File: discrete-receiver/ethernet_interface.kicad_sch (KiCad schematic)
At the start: 16 parts, among them J6 SI-52003-F, U9 LAN8720A

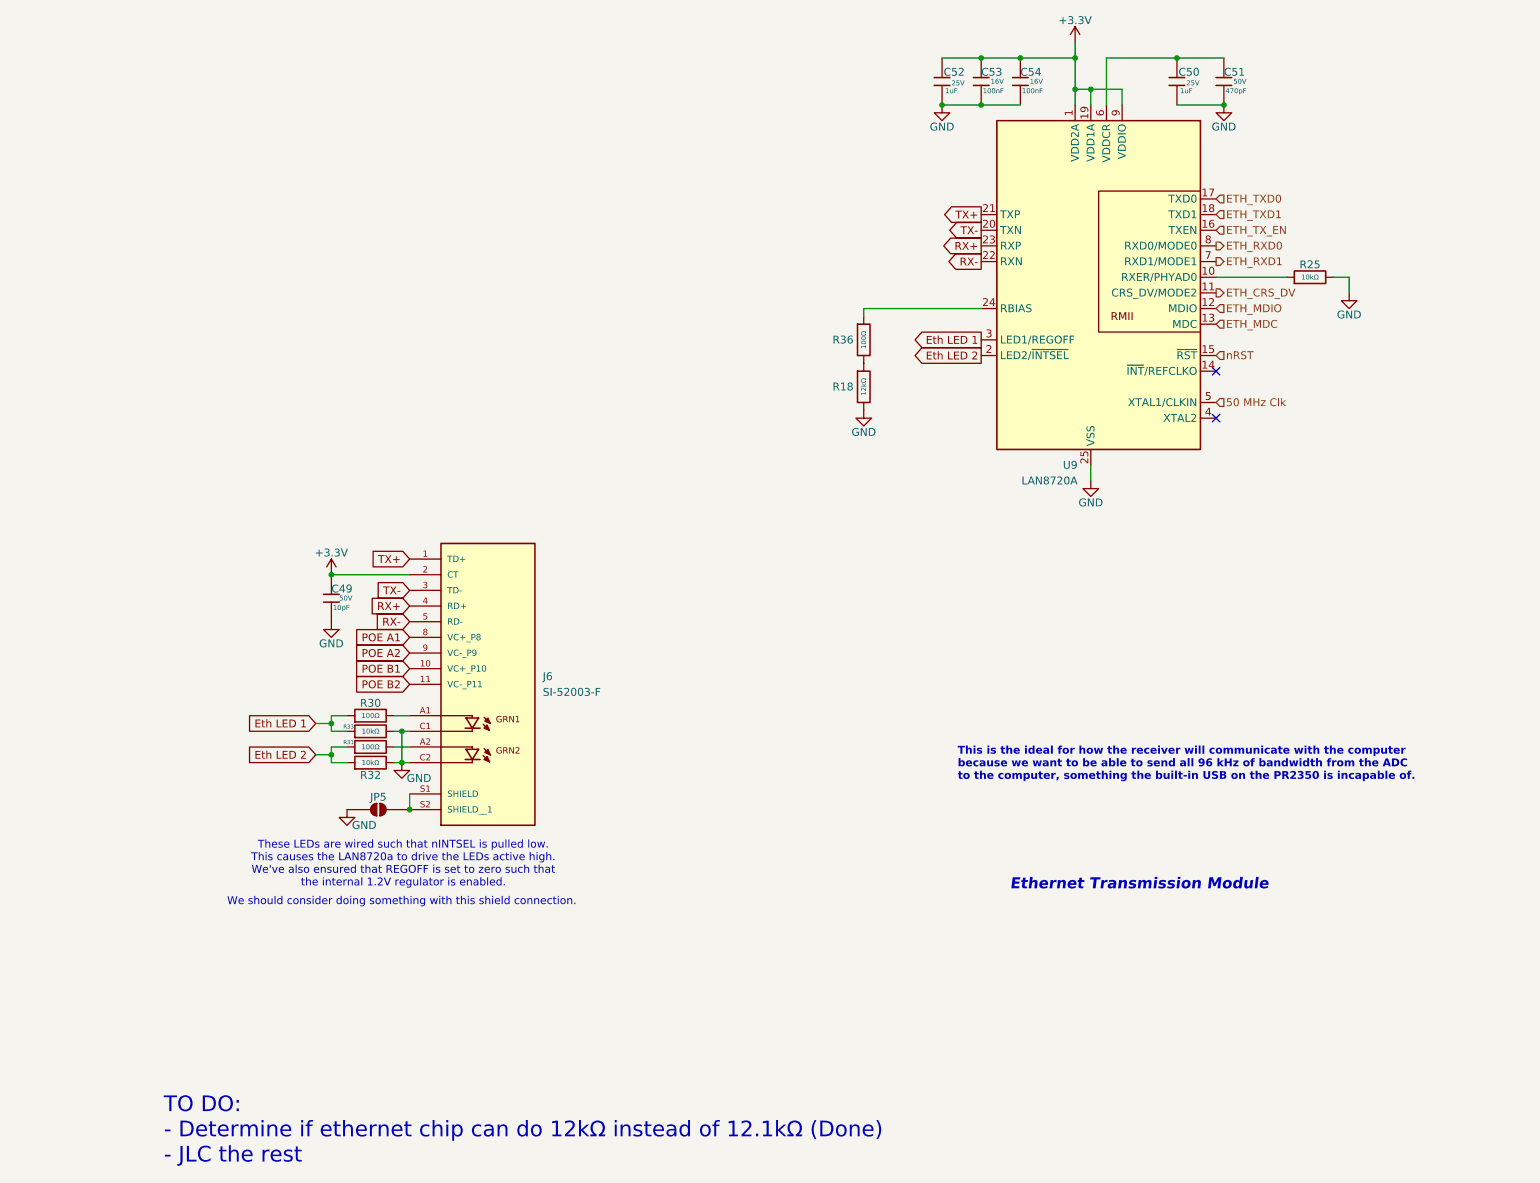
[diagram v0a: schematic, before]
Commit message: Updated JLC part numbers because some parts were out of stock
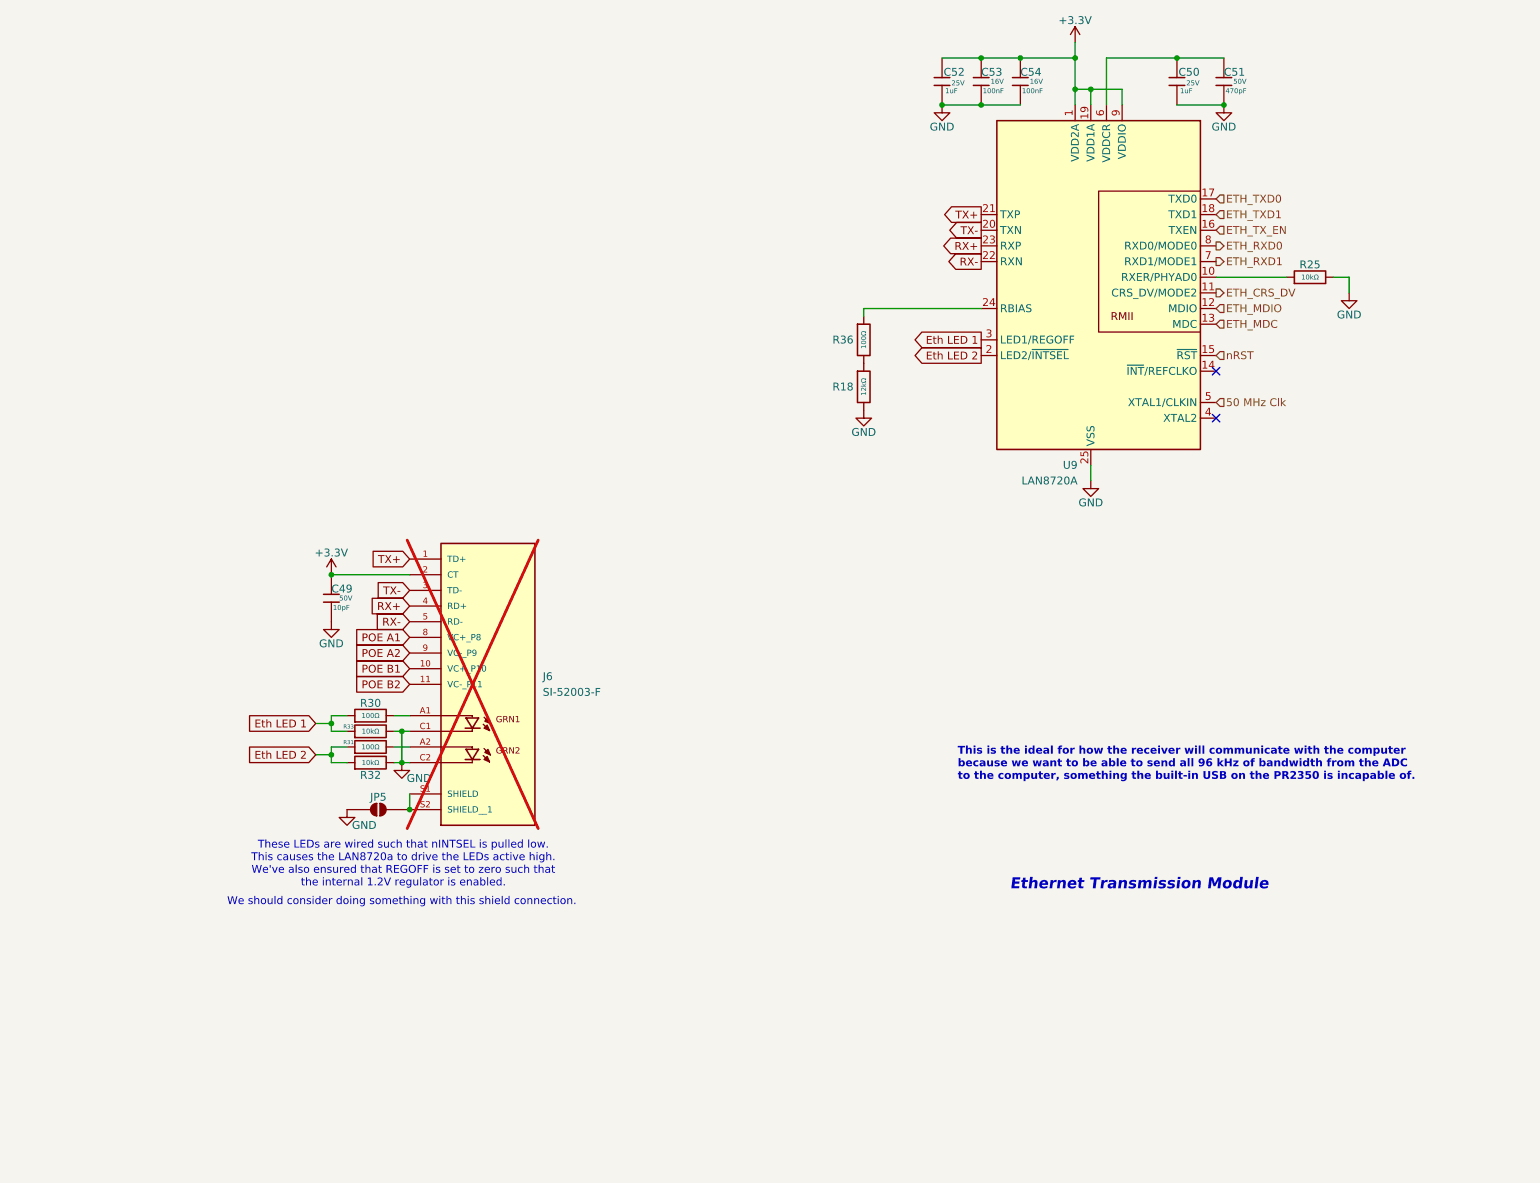
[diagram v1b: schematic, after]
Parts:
- J6: now not fitted; now left out of the parts list
- U9: LCSC (none) -> C17146
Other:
- note removed: "TO DO: - Determine if ethernet chip can do 12kΩ instead of 12.1kΩ (Done) - JLC the rest"
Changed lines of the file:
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@@
-		)
-	)
-	(text "TO DO:\n- Determine if ethernet chip can do 12kΩ instead of 12.1kΩ (Done)\n- JLC the rest"
-		(exclude_from_sim no)
-		(at 49.022 229.87 0)
-		(effects
-			(font
-				(size 2.54 2.54)
-			)
-			(justify left)
 		)
 	)
@@
 		(body_style 1)
 		(exclude_from_sim no)
-		(in_bom yes)
+		(in_bom no)
 		(on_board yes)
-		(in_pos_files yes)
-		(dnp no)
+		(in_pos_files no)
+		(dnp yes)
 		(fields_autoplaced yes)
 		(property "Reference" "J6"
@@
 			(at 199.39 93.98 0)
 			(hide yes)
+			(show_name no)
+			(do_not_autoplace no)
+			(effects
+				(font
+					(size 1.27 1.27)
+				)
+			)
+		)
+		(property "LCSC" "C17146"
+			(at 199.39 93.98 0)
+			(hide yes)

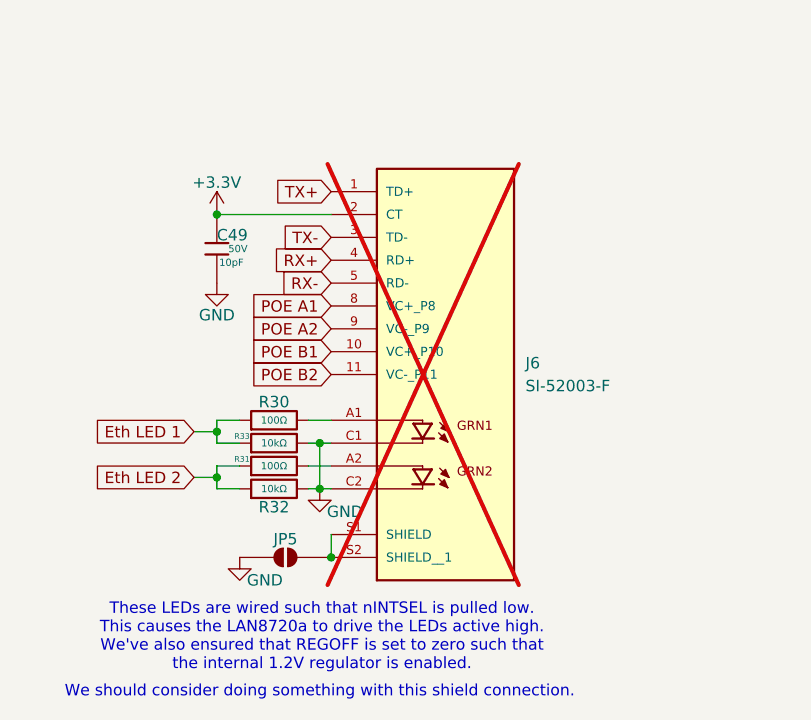
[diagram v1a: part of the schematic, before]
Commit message: replaced RJ45 connector 😡🙄🥀
The original was too expensive from JLCPCB and Digikey.
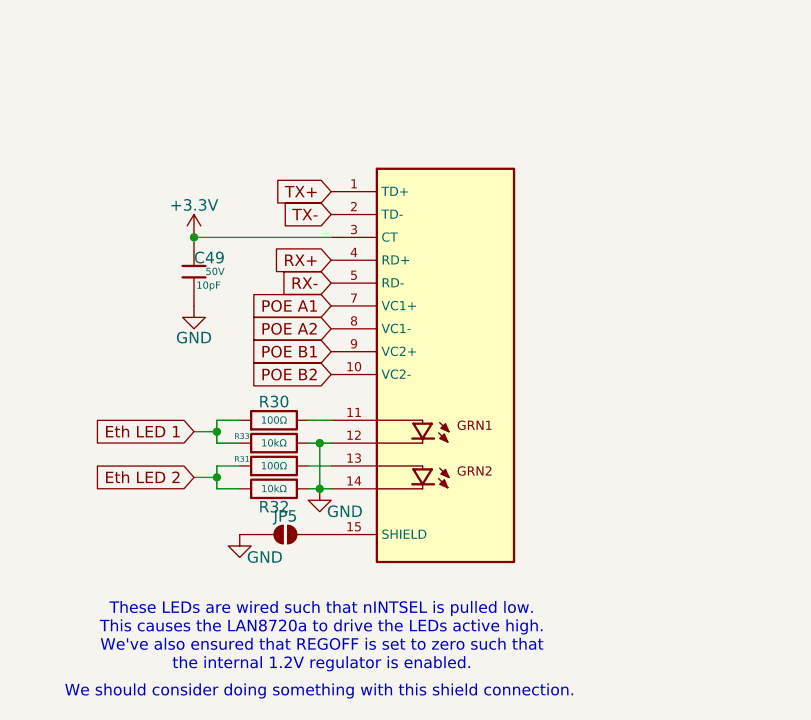
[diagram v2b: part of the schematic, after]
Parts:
- removed J6: SI-52003-F, sdr_project:BEL_SI-52003-F, symbol SI-52003-F:SI-52003-F
- added RJ1: (no value), EasyEDA_Lib:RJ45-TH_HR873168AE, symbol EasyEDA_Lib:HR873168AE
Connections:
- net +3.3V: now also RJ1.3 (CT)
- net GND: now also RJ1.12, RJ1.14
- net POE A1: now also RJ1.7 (VC1+)
- net POE A2: now also RJ1.8 (VC1-)
- net POE B1: now also RJ1.9 (VC2+)
- net POE B2: now also RJ1.10 (VC2-)
- net RX+: now also RJ1.4 (RD+)
- net RX-: now also RJ1.5 (RD-)
- net TX+: now also RJ1.1 (TD+)
- net TX-: now also RJ1.2 (TD-)
- net at JP5.2 (B): now also RJ1.15 (SHIELD), RJ1.16 (SHIELD)
- net at R31.2: now also RJ1.13
- net at R30.2: now also RJ1.11
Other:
- moved on the sheet: C49, JP5

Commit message: Fixed PCB component rotation offsets
A few components needed to get a rotation offset for JLCPCB production. Also more silkscreen content was added.
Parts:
- U9: Rotation Offset (none) -> 270
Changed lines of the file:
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@@
+			)
+		)
+		(property "Rotation Offset" "270"
+			(at 199.39 93.98 0)
+			(hide yes)
+			(show_name no)
+			(do_not_autoplace no)
+			(effects
+				(font
+					(size 1.27 1.27)
+				)
 			)
 		)

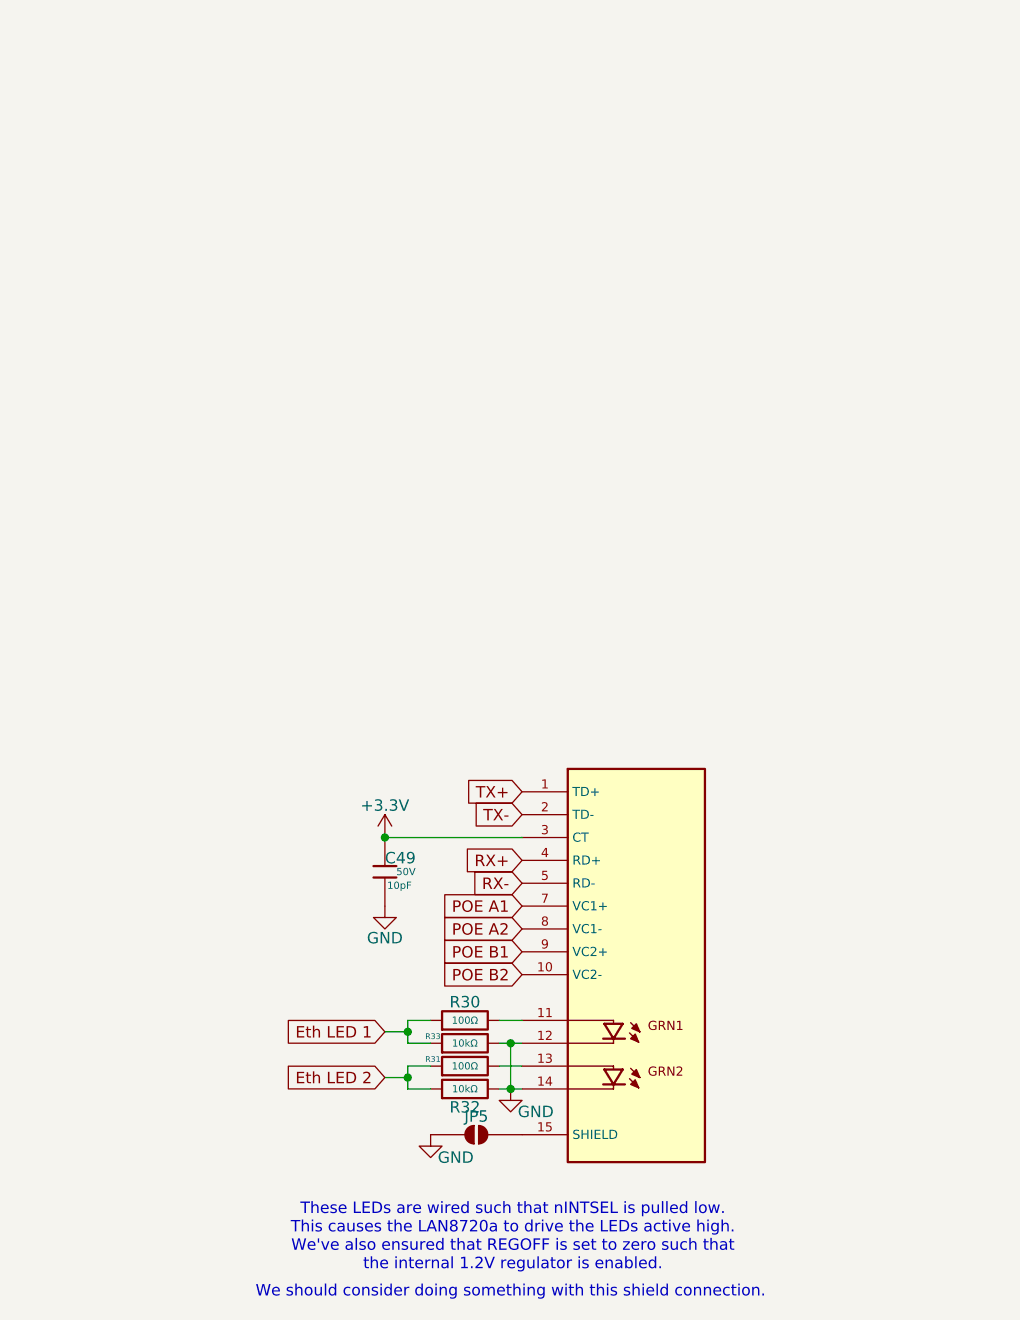
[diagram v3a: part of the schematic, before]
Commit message: Added/Modified/Deleted Schematic Notes
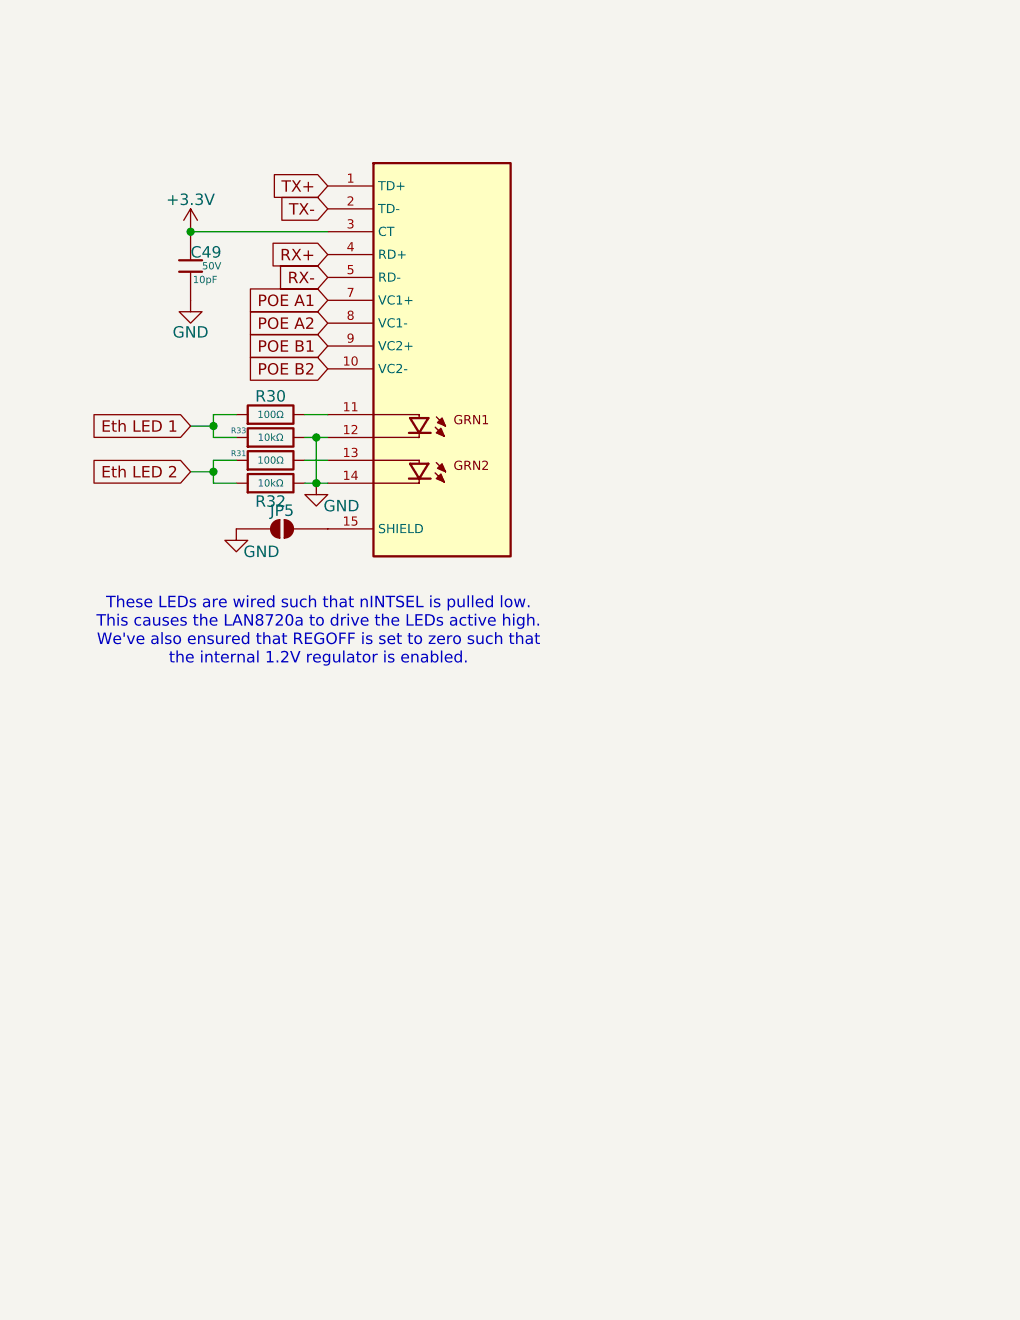
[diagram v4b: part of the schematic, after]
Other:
- note removed: "We should consider doing something with this shield connection."
- moved on the sheet: C49, JP5, R30, R31, R32, R33

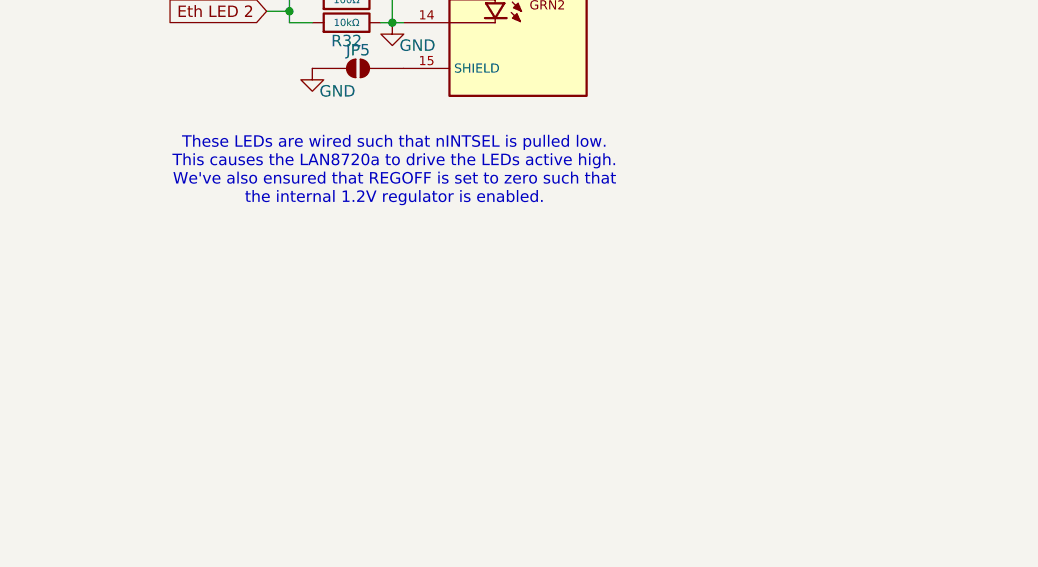
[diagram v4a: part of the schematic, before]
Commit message: Added note about ethernet LED strapping error
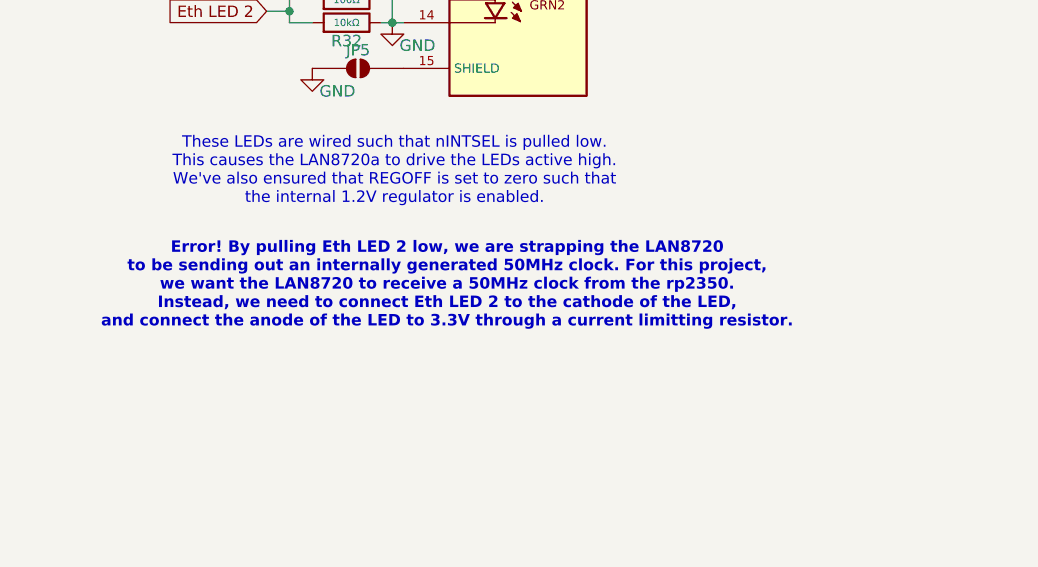
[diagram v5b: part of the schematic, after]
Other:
- note added: "Error! By pulling Eth LED 2 low, we are strapping the LAN8720 to be sending out an internally generated 50MHz clock. For this project, we want the LAN8720 to receive a 50MHz clock from the rp2350. Instead, we need to connect Eth LED 2 to the cathode of the LED, and connect the anode of the LED to 3.3V through a current limitting resistor."
